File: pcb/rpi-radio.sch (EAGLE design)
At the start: 21 parts, among them SW1 EC12E_SW, SW2 EC12E_SW, U1 TDA7052B, U2 TDA7052B

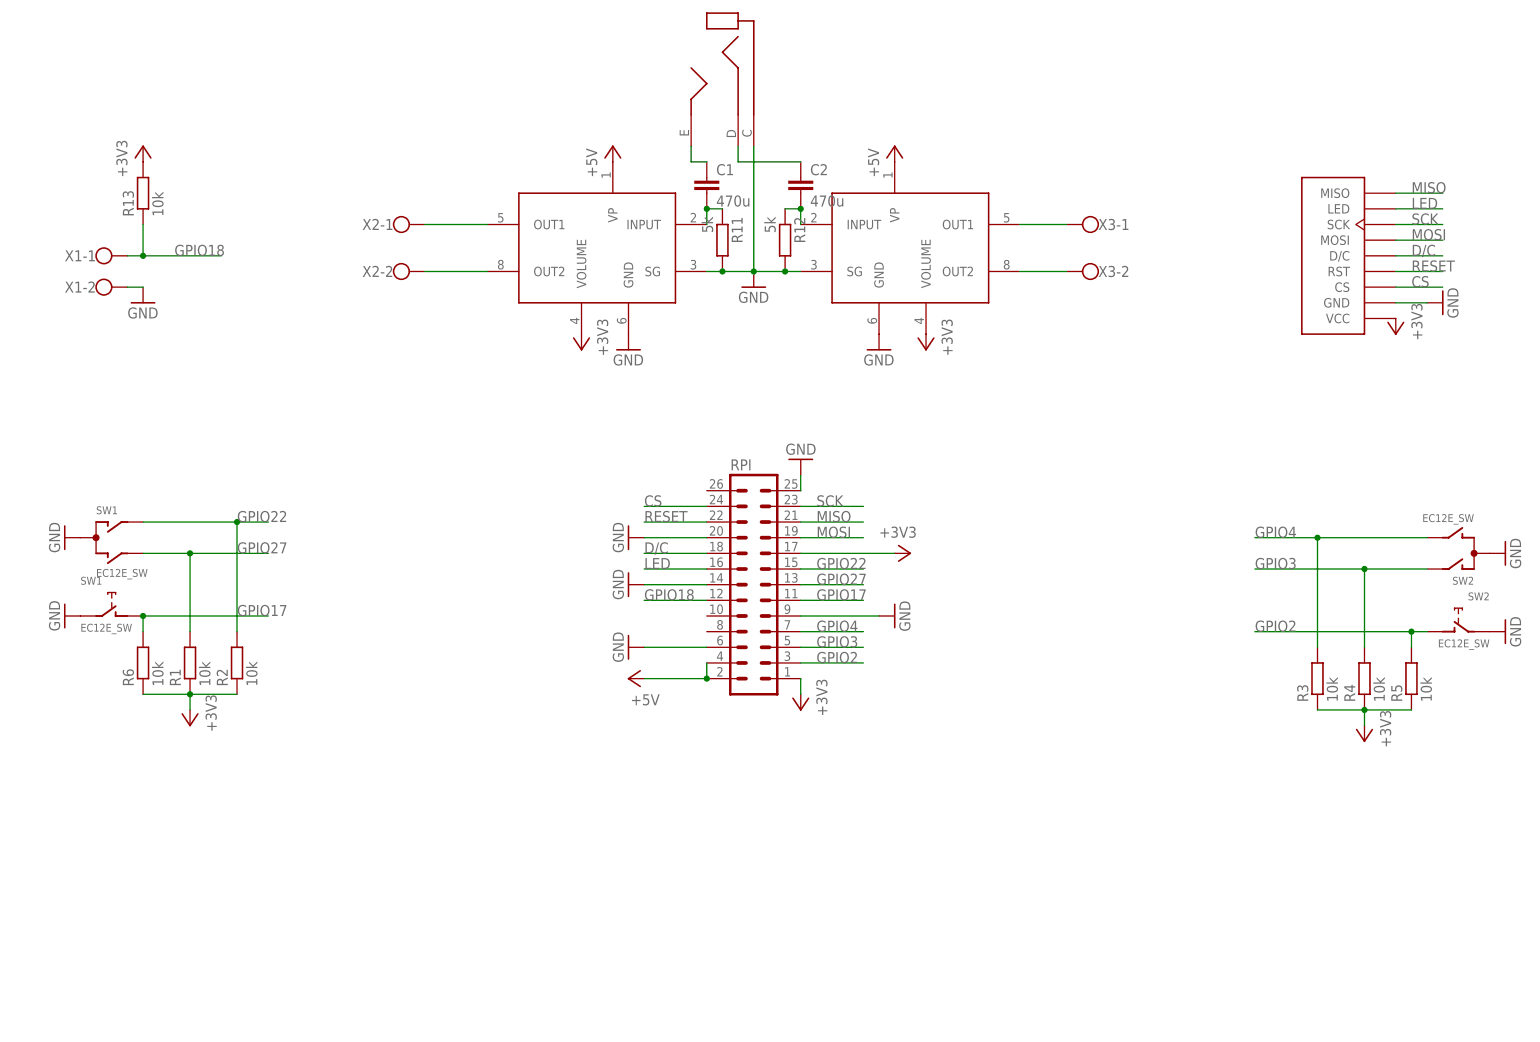
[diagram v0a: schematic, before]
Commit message: pcb: add attiny2313, because rpi is not able to decode the rotary encoder and use thicker traces
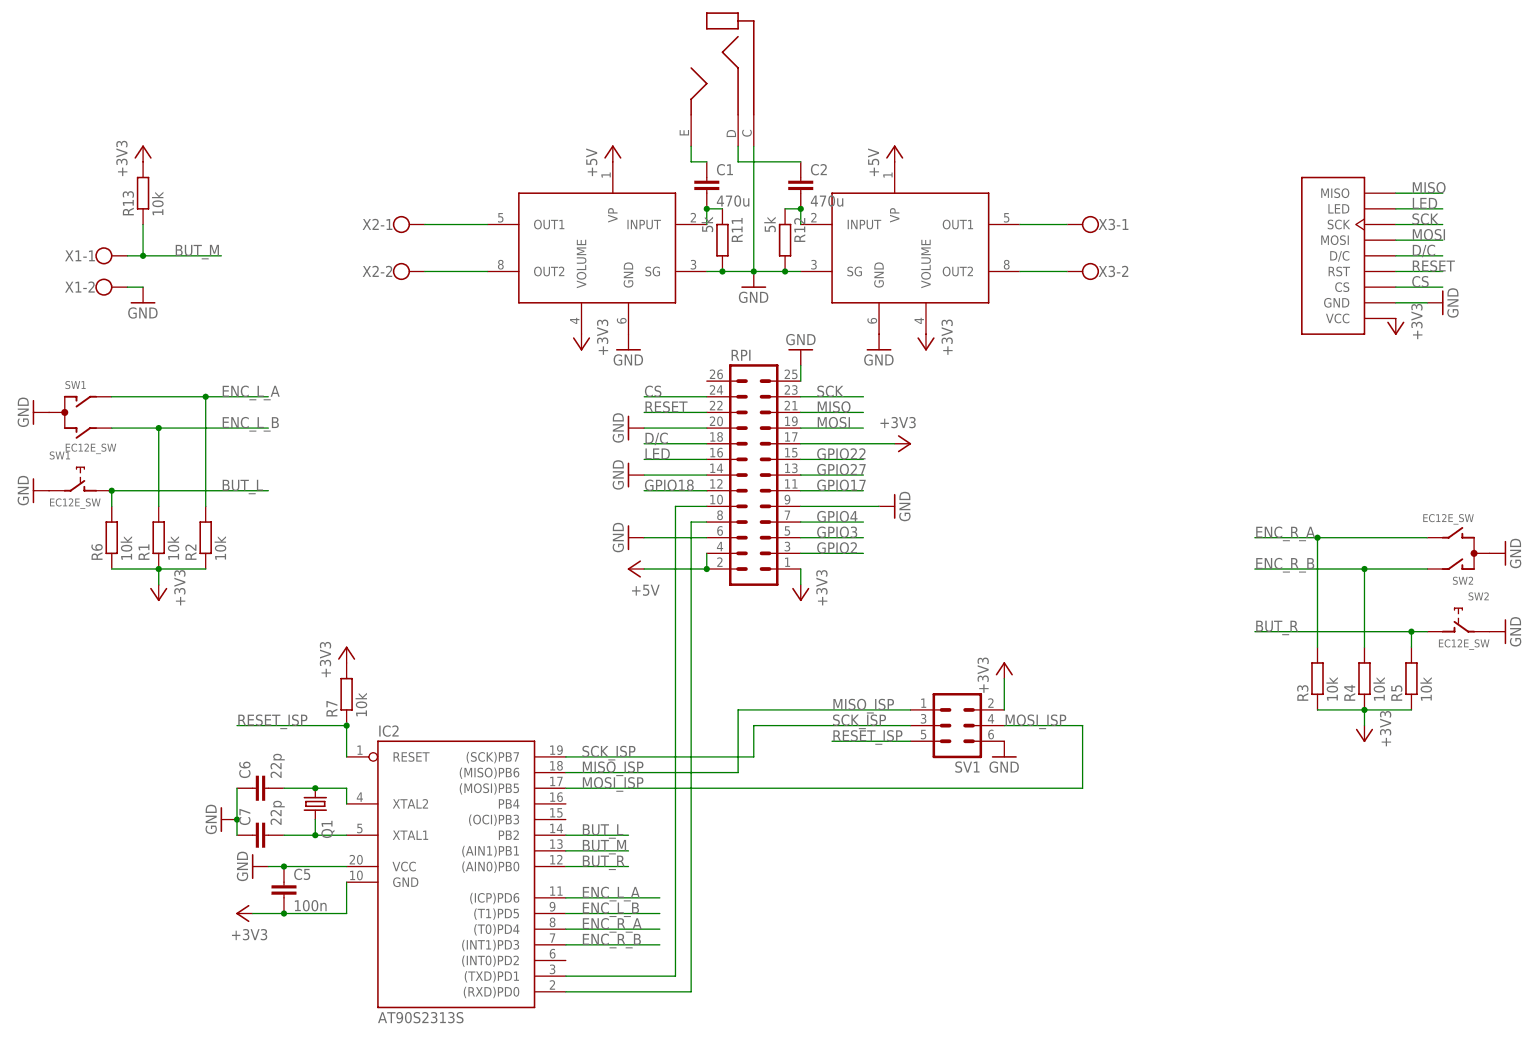
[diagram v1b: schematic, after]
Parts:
- added C5: 100n, resistor:C-EUC0805
- added C6, C7: 22p, resistor:C-EUC0805
- added IC2: AT90S2313S, atmel:AT90S2313S
- added Q1: (no value), crystal:CRYSTALHC49S
- added R7: 10k, resistor:R-EU_M0805
- added SV1: (no value), con-ml:ML6
- R1, R11, R12, R13, R2, R3, R4, R5, R6: device resistor:R-EU_0204/5 -> resistor:R-EU_R0805
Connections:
- new net BUT_L: IC2.PB2, R6.2, SW1G$2.1
- new net BUT_M: IC2.(AIN1)PB1, R13.1, X1-1.KL
- new net BUT_R: IC2.(AIN0)PB0, R5.2, SW2G$2.1
- new net ENC_L_A: IC2.(ICP)PD6, R2.2, SW1G$1.A
- new net ENC_L_B: IC2.(T1)PD5, R1.2, SW1G$1.B
- new net ENC_R_A: IC2.(T0)PD4, R3.2, SW2G$1.B
- new net ENC_R_B: IC2.(INT1)PD3, R4.2, SW2G$1.A
- new net MISO_ISP: IC2.(MISO)PB6, SV1.1
- new net MOSI_ISP: IC2.(MOSI)PB5, SV1.4
- new net N$10: C6.2, IC2.XTAL2, Q1.1
- new net N$13: IC2.(RXD)PD0, RPI.8
- new net N$14: IC2.(TXD)PD1, RPI.10
- new net N$15: C7.2, IC2.XTAL1, Q1.2
- new net RESET_ISP: IC2.RESET, R7.1, SV1.5
- new net SCK_ISP: IC2.(SCK)PB7, SV1.3
- net +3V3: now also C5.2, IC2.GND, R7.2, SV1.2
- net GND: now also C5.1, C6.1, C7.1, IC2.VCC, SV1.6
- net GPIO17: no longer R6.2, SW1G$2.1
- net GPIO18: no longer R13.1, X1-1.KL
- net GPIO2: no longer R5.2, SW2G$2.1
- net GPIO22: no longer R2.2, SW1G$1.A
- net GPIO27: no longer R1.2, SW1G$1.B
- net GPIO3: no longer R4.2, SW2G$1.A
- net GPIO4: no longer R3.2, SW2G$1.B
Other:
- moved on the sheet: R1, R2, R6, RPI, SW1

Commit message: Update to version v2 of the pcb. the integrated amplifier did not work properly
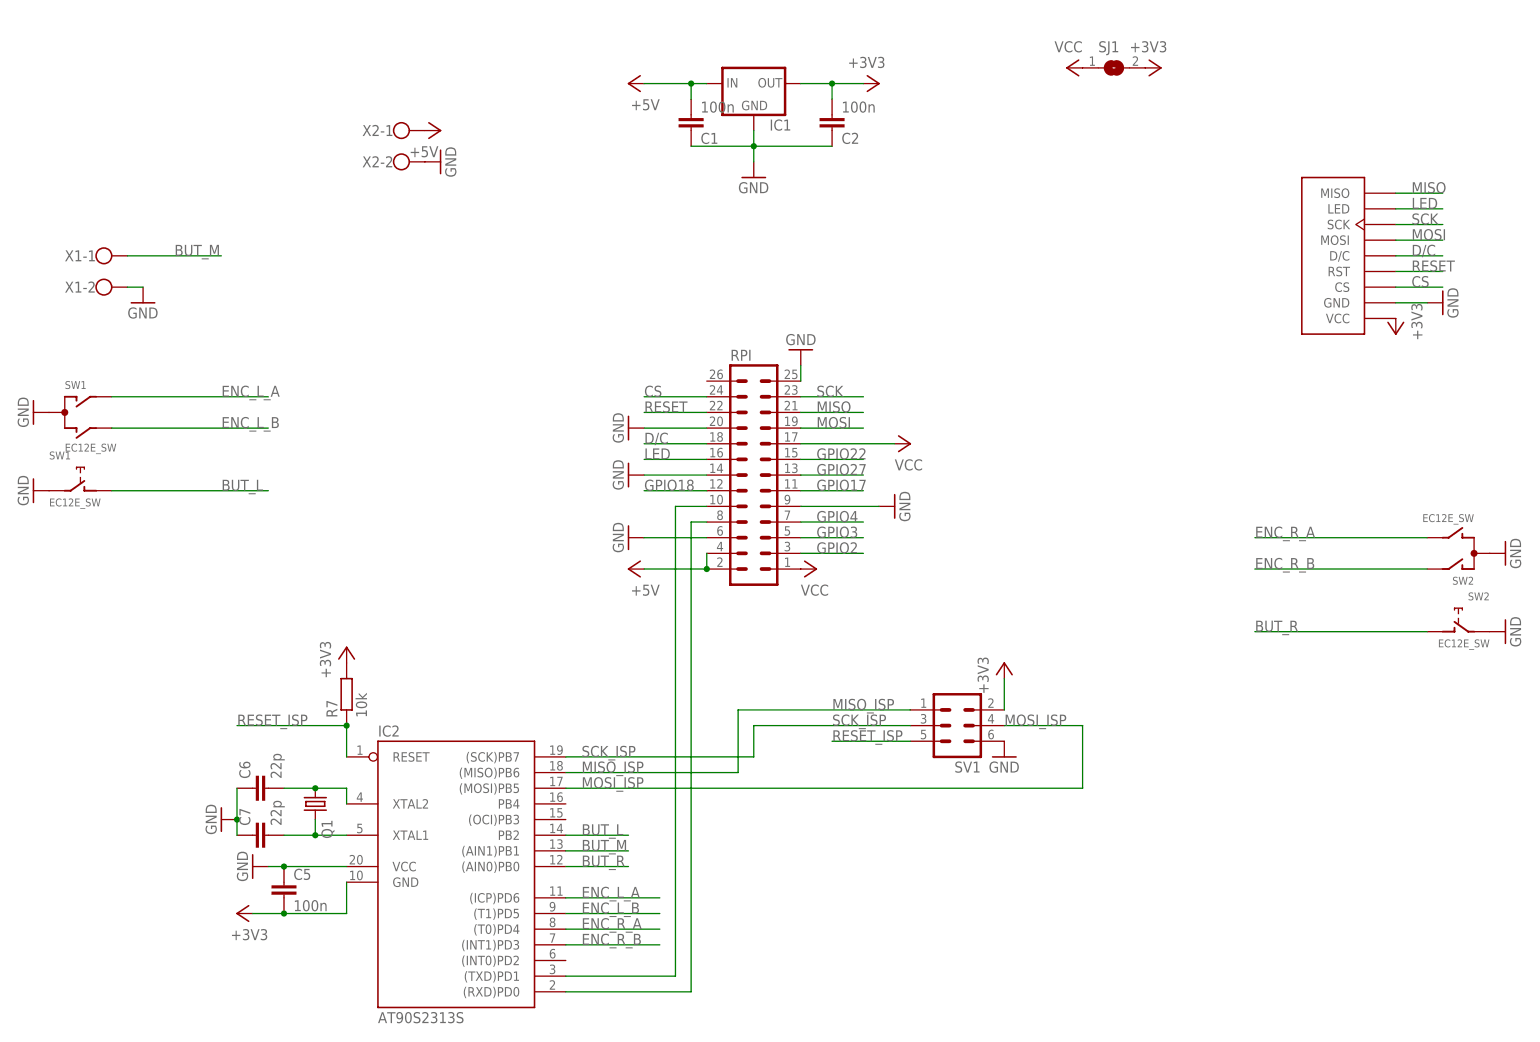
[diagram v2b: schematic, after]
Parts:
- removed R1, R13, R2, R3, R4, R5, R6: 10k, resistor:R-EU_R0805
- removed R11, R12: 5k, resistor:R-EU_R0805
- removed U$5: JACK3.5, rpi-radio:JACK3.5
- removed U1, U2: TDA7052B, tda7052b:TDA7052B
- removed X3: (no value), con-wago-500:W237-102
- added IC1: (no value), v-reg:78XXS
- added SJ1: (no value), jumper:SJ
- C1, C2: value 470u -> 100n; device resistor:C-EU025-030X050 -> resistor:C-EUC0805
- SW1, SW2: device switch-alps:EC12E_SW -> rpi-radio:EC12E_SW
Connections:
- removed net N$1: C2.2, R12.1, U2.INPUT
- removed net N$2: C1.2, R11.1, U1.INPUT
- removed net N$3: C1.1, U$5.E
- removed net N$4: U1.OUT1, X2-1.KL
- removed net N$5: U1.OUT2, X2-2.KL
- removed net N$6: U2.OUT1, X3-1.KL
- removed net N$7: U2.OUT2, X3-2.KL
- removed net N$8: C2.1, U$5.D
- new net VCC: RPI.1, RPI.17, SJ1.1
- net +3V3: now also C2.2, IC1.OUT, SJ1.2; no longer R1.1, R13.2, R2.1, R3.1, R4.1, R5.1, R6.1, RPI.1, RPI.17, U1.VOLUME, U2.VOLUME
- net +5V: now also C1.2, IC1.IN, X2-1.KL; no longer U1.VP, U2.VP
- net BUT_L: no longer R6.2
- net BUT_M: no longer R13.1
- net BUT_R: no longer R5.2
- net ENC_L_A: no longer R2.2
- net ENC_L_B: no longer R1.2
- net ENC_R_A: no longer R3.2
- net ENC_R_B: no longer R4.2
- net GND: now also C1.1, C2.1, IC1.GND, X2-2.KL; no longer R11.2, R12.2, U$5.C, U1.GND, U1.SG, U2.GND, U2.SG
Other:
- moved on the sheet: C1, C2, X2-1, X2-2

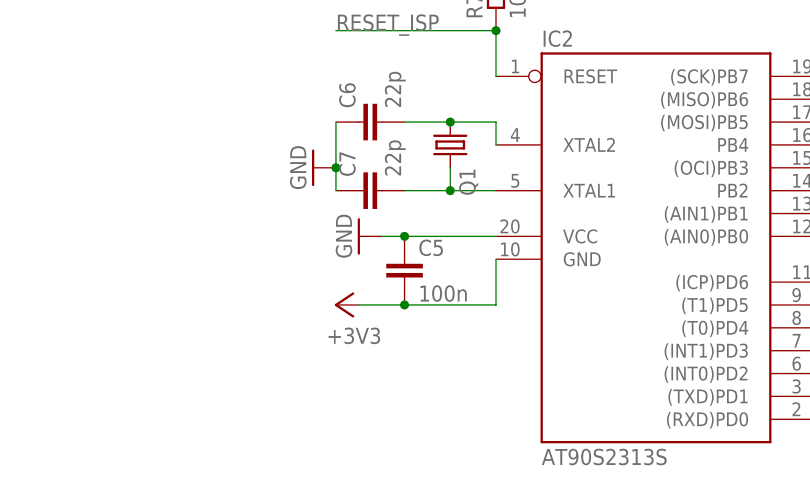
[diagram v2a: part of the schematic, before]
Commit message: Fix wrong polarity of attiny
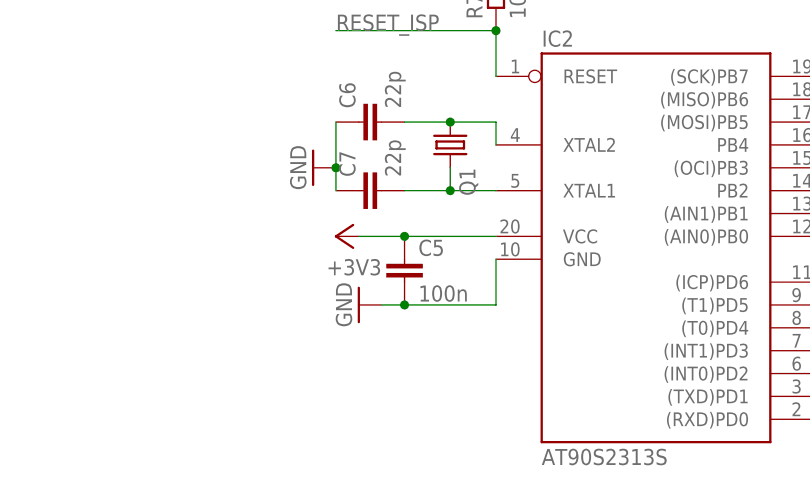
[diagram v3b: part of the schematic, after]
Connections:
- net +3V3: now also C5.1, IC2.VCC; no longer C5.2, IC2.GND
- net GND: now also C5.2, IC2.GND; no longer C5.1, IC2.VCC
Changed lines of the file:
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@@
 <?xml version="1.0" encoding="utf-8"?>
 <!DOCTYPE eagle SYSTEM "eagle.dtd">
-<eagle version="6.6.0">
+<eagle version="7.2.0">
 <drawing>
 <settings>
@@
 <instance part="+3V9" gate="G$1" x="60.96" y="68.58"/>
 <instance part="GND9" gate="1" x="40.64" y="40.64" rot="R270"/>
-<instance part="+3V10" gate="G$1" x="43.18" y="25.4" rot="R90"/>
-<instance part="GND16" gate="1" x="45.72" y="33.02" rot="R270"/>
+<instance part="+3V10" gate="G$1" x="43.18" y="33.02" rot="R90"/>
+<instance part="GND16" gate="1" x="45.72" y="25.4" rot="R270"/>
 <instance part="C5" gate="G$1" x="50.8" y="30.48"/>
 <instance part="C6" gate="G$1" x="45.72" y="45.72" rot="R90"/>
@@
 </segment>
 <segment>
-<pinref part="C5" gate="G$1" pin="1"/>
-<pinref part="IC2" gate="G$1" pin="VCC"/>
-<wire x1="50.8" y1="33.02" x2="60.96" y2="33.02" width="0.1524" layer="91"/>
-<wire x1="50.8" y1="33.02" x2="48.26" y2="33.02" width="0.1524" layer="91"/>
-<pinref part="GND16" gate="1" pin="GND"/>
-<junction x="50.8" y="33.02"/>
-</segment>
-<segment>
 <pinref part="IC1" gate="1" pin="GND"/>
 <pinref part="GND1" gate="1" pin="GND"/>
@@
 <pinref part="GND2" gate="1" pin="GND"/>
 </segment>
+<segment>
+<pinref part="C5" gate="G$1" pin="2"/>
+<pinref part="GND16" gate="1" pin="GND"/>
+<wire x1="48.26" y1="25.4" x2="50.8" y2="25.4" width="0.1524" layer="91"/>
+<pinref part="IC2" gate="G$1" pin="GND"/>
+<wire x1="60.96" y1="30.48" x2="60.96" y2="25.4" width="0.1524" layer="91"/>
+<wire x1="50.8" y1="25.4" x2="60.96" y2="25.4" width="0.1524" layer="91"/>
+<junction x="50.8" y="25.4"/>
+</segment>
 </net>
 <net name="+3V3" class="0">
@@
 <pinref part="+3V12" gate="G$1" pin="+3V3"/>
 <wire x1="167.64" y1="58.42" x2="167.64" y2="63.5" width="0.1524" layer="91"/>
-</segment>
-<segment>
-<pinref part="IC2" gate="G$1" pin="GND"/>
-<wire x1="60.96" y1="30.48" x2="60.96" y2="25.4" width="0.1524" layer="91"/>
-<pinref part="C5" gate="G$1" pin="2"/>
-<wire x1="60.96" y1="25.4" x2="50.8" y2="25.4" width="0.1524" layer="91"/>
-<wire x1="50.8" y1="25.4" x2="45.72" y2="25.4" width="0.1524" layer="91"/>
-<pinref part="+3V10" gate="G$1" pin="+3V3"/>
-<junction x="50.8" y="25.4"/>
 </segment>
 <segment>
@@
 <pinref part="+3V1" gate="G$1" pin="+3V3"/>
 </segment>
+<segment>
+<pinref part="+3V10" gate="G$1" pin="+3V3"/>
+<pinref part="C5" gate="G$1" pin="1"/>
+<wire x1="45.72" y1="33.02" x2="50.8" y2="33.02" width="0.1524" layer="91"/>
+<pinref part="IC2" gate="G$1" pin="VCC"/>
+<wire x1="50.8" y1="33.02" x2="60.96" y2="33.02" width="0.1524" layer="91"/>
+<junction x="50.8" y="33.02"/>
+</segment>
 </net>
